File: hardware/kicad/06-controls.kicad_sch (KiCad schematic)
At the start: 38 parts, among them SW1 UP, SW10 SELECT, SW11 L, SW12 R, SW13 MENU, SW2 DOWN, SW3 LEFT, SW4 RIGHT, SW5 A, SW6 B, SW7 X, SW8 Y, SW9 START

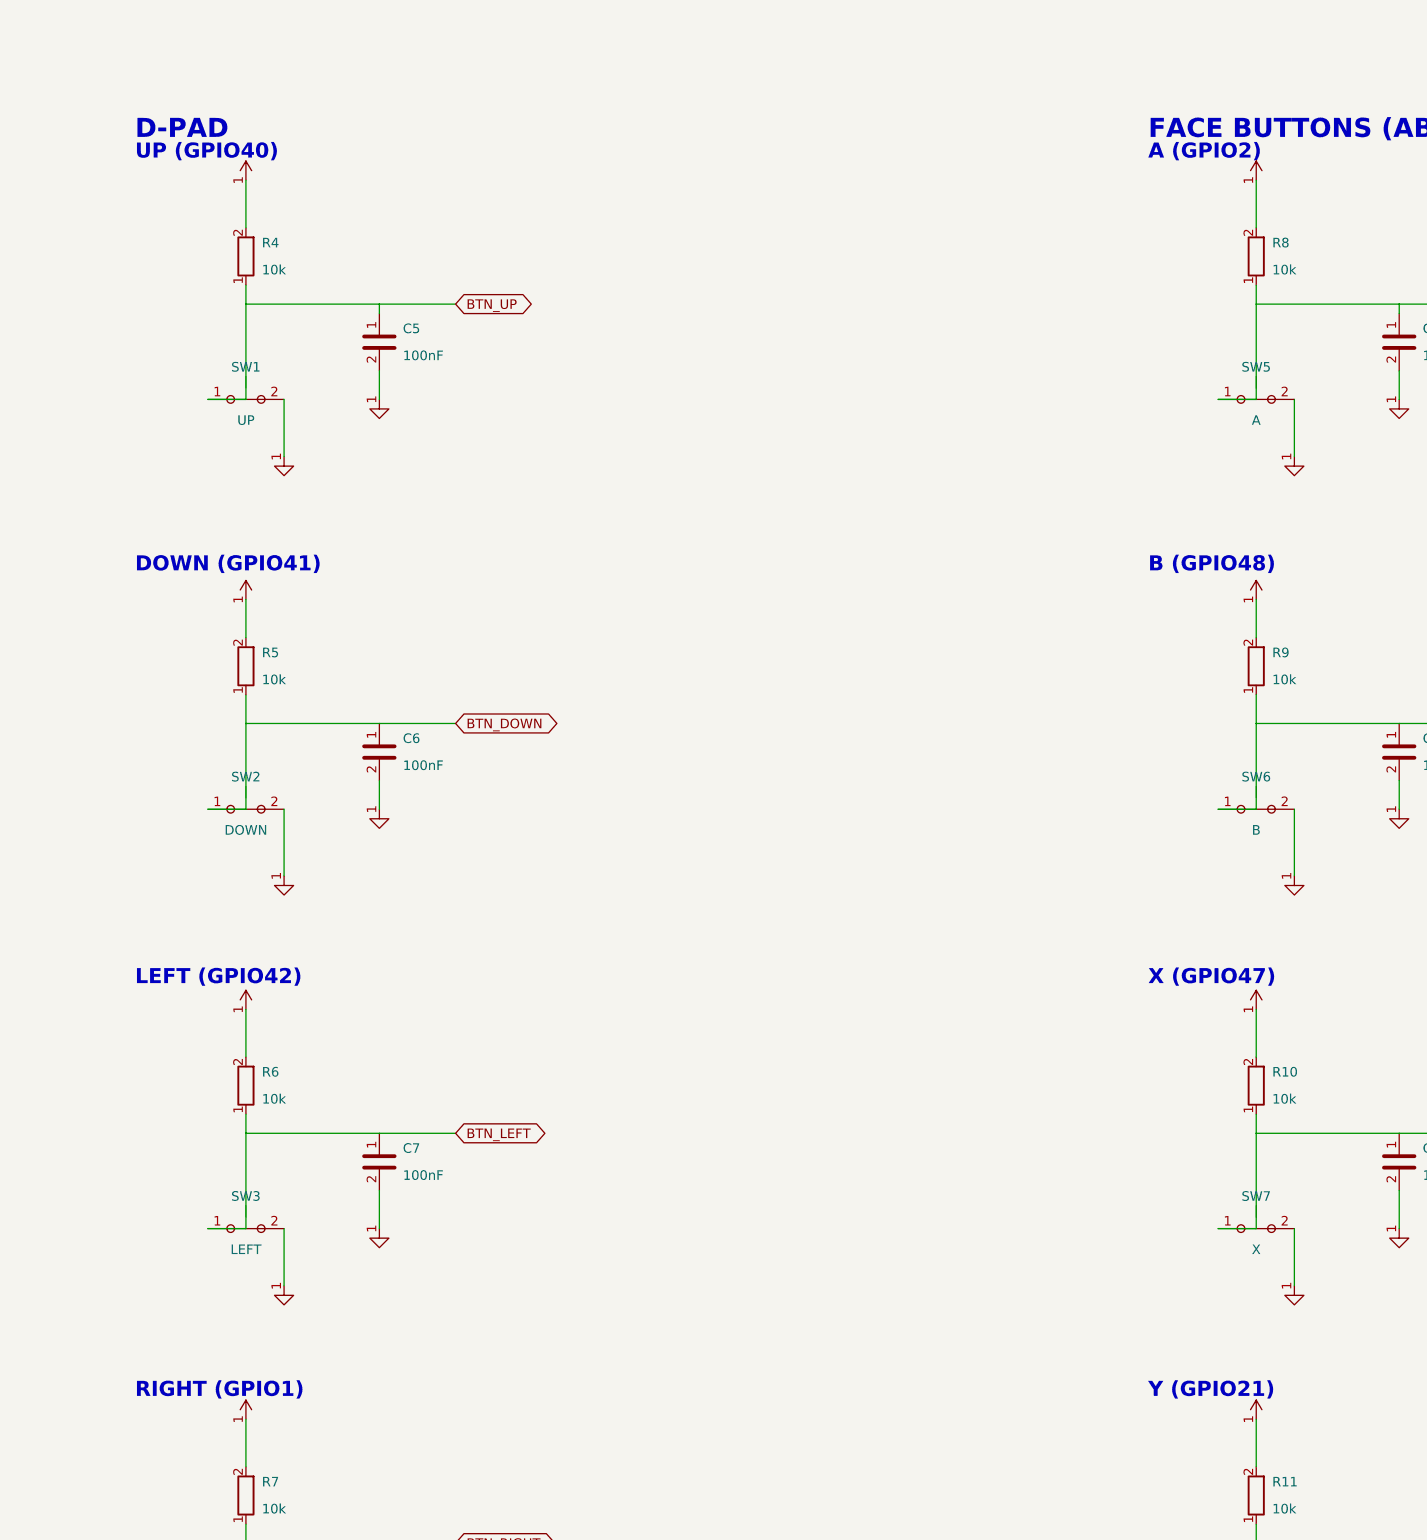
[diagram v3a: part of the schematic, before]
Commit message: Retro-Go first boot on the first article + R39-HIGH-1 (module pins 38/39 swapped)
Phase 2.8 reached: Retro-Go runs on article 0003 — launcher, SD, all 12
buttons, Owlia (NES) and Mario Bros played. Fork fixes are in the
submodule (0e533078, 53878dcb): i80 0x2C/0x3C continuation, landscape
480x320, PDM channel off at volume 0, RIGHT/A swap, L/R in the launcher.

R39-HIGH-1: the WROOM-1 datasheet has pin 38 = IO2 and pin 39 = IO1;
every project table (generator _PIN_TO_GPIO, datasheet_specs, schematic
pin table + symbol, board_config.h, Retro-Go target) had them swapped,
and verify_dfm_v2 asserted the wrong fact. Pins 4-37 re-verified against
the datasheet: only this pair. The copper is right — BTN_RIGHT is on pad
38 = GPIO2, BTN_A on pad 39 = GPIO1 — so the fix is names only:
BTN_RIGHT=GPIO2, BTN_A=GPIO1 everywhere; the regenerated PCB is
byte-identical to the built board; schematics, symbol, bring-up firmware,
net-explorer data and docs regenerated. Gate now asserts 38=GPIO2 and
39=GPIO1. verify-all green, verify_dfa 10/10, retro-go sync 63/63.

Also: prebuilt Retro-Go binaries refreshed, Phase 2 docs switched to
landscape scaling, .gitignore keeps every ROM under test-roms/ out of git
except the committed homebrew set, session log extended.

Co-Authored-By: Claude Opus 5 (1M context) <noreply@anthropic.com>
Claude-Session: https://claude.ai/code/session_01MsWyvkWxko6nCK1kvUkZjV
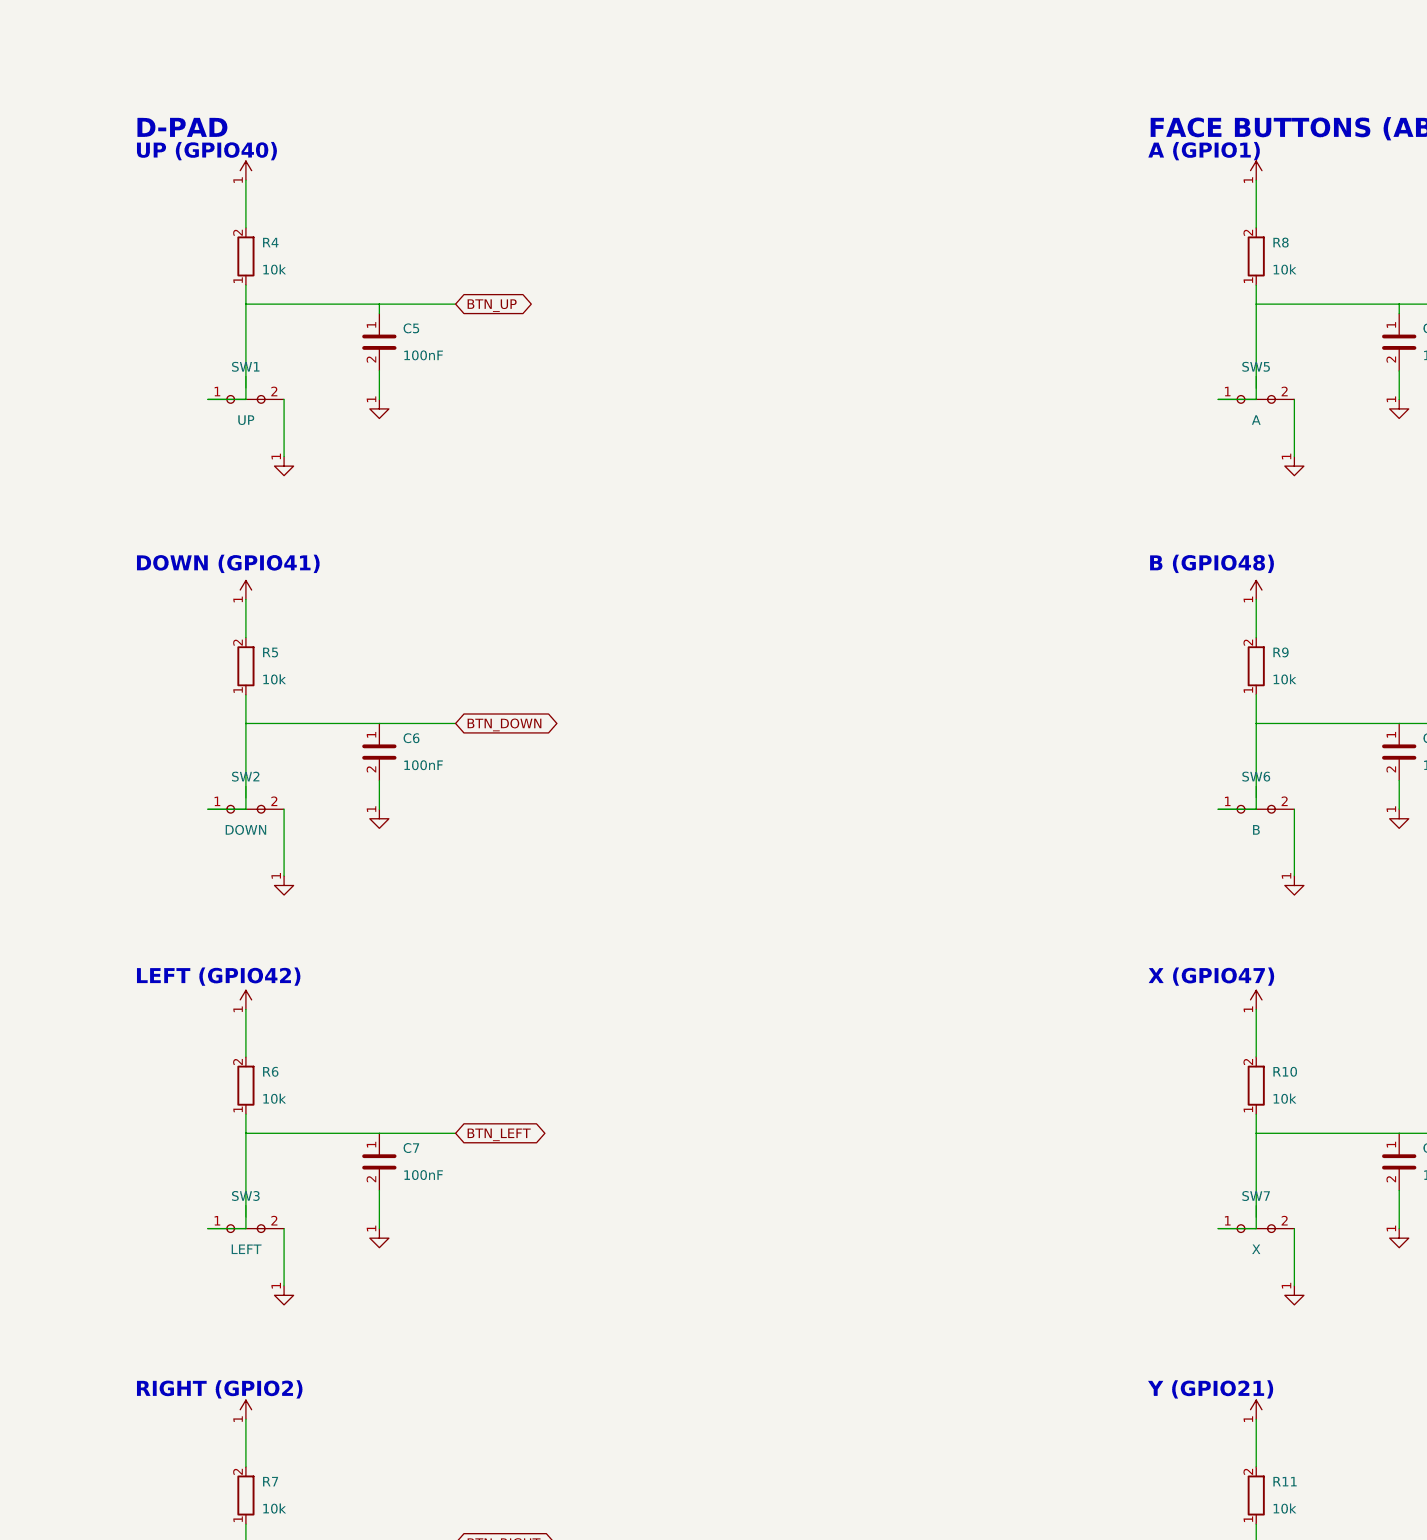
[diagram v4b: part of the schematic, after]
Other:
- note added: "A (GPIO1)"
- note added: "RIGHT (GPIO2)"
- note removed: "A (GPIO2)"
- note removed: "RIGHT (GPIO1)"
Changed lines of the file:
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@@
   (global_label "BTN_LEFT" (shape bidirectional) (at 92.71 186.69 0) (effects (font (size 1.27 1.27))) (property "Intersheetrefs" "" (at 0 0 0) (effects (font (size 1.27 1.27)) hide)))
   (wire (pts (xy 82.55 186.69) (xy 92.71 186.69)) (stroke (width 0) (type default)))
-  (text "RIGHT (GPIO1)" (at 50 221 0) (effects (font (size 2 2) bold) (justify left)))
+  (text "RIGHT (GPIO2)" (at 50 221 0) (effects (font (size 2 2) bold) (justify left)))
   (symbol (lib_id "emu:R") (at 64.77 234.95 180) (unit 1) (exclude_from_sim no) (in_bom yes) (on_board yes) (dnp no) (property "Reference" "R7" (at 66.89 233.15 0) (effects (font (size 1.27 1.27)) (justify right))) (property "Value" "10k" (at 66.89 236.75 0) (effects (font (size 1.27 1.27)) (justify right))) (pin "1") (pin "2") (instances (project "esp32-emu-turbo" (path "/00000007-cafe-4000-8000-000000000007" (reference "R7") (unit 1)) (path "/00000001-cafe-4000-8000-000000000001/00000007-cafe-4000-8000-000000000007" (reference "R7") (unit 1)))))
   (symbol (lib_id "emu:+3V3") (at 64.77 224.79 0) (unit 1) (exclude_from_sim no) (in_bom no) (on_board no) (dnp no) (property "Reference" "#PWR010" (at 64.77 222.79 0) (effects (font (size 1.27 1.27)) hide)) (property "Value" "+3V3" (at 64.77 226.79 0) (effects (font (size 1.27 1.27)) hide)) (pin "1") (instances (project "esp32-emu-turbo" (path "/00000007-cafe-4000-8000-000000000007" (reference "#PWR010") (unit 1)) (path "/00000001-cafe-4000-8000-000000000001/00000007-cafe-4000-8000-000000000007" (reference "#PWR010") (unit 1)))))
@@
   (global_label "BTN_RIGHT" (shape bidirectional) (at 92.71 241.3 0) (effects (font (size 1.27 1.27))) (property "Intersheetrefs" "" (at 0 0 0) (effects (font (size 1.27 1.27)) hide)))
   (wire (pts (xy 82.55 241.3) (xy 92.71 241.3)) (stroke (width 0) (type default)))
-  (text "A (GPIO2)" (at 185 56 0) (effects (font (size 2 2) bold) (justify left)))
+  (text "A (GPIO1)" (at 185 56 0) (effects (font (size 2 2) bold) (justify left)))
   (symbol (lib_id "emu:R") (at 199.39 69.85 180) (unit 1) (exclude_from_sim no) (in_bom yes) (on_board yes) (dnp no) (property "Reference" "R8" (at 201.51 68.05 0) (effects (font (size 1.27 1.27)) (justify right))) (property "Value" "10k" (at 201.51 71.65 0) (effects (font (size 1.27 1.27)) (justify right))) (pin "1") (pin "2") (instances (project "esp32-emu-turbo" (path "/00000007-cafe-4000-8000-000000000007" (reference "R8") (unit 1)) (path "/00000001-cafe-4000-8000-000000000001/00000007-cafe-4000-8000-000000000007" (reference "R8") (unit 1)))))
   (symbol (lib_id "emu:+3V3") (at 199.39 59.69 0) (unit 1) (exclude_from_sim no) (in_bom no) (on_board no) (dnp no) (property "Reference" "#PWR013" (at 199.39 57.69 0) (effects (font (size 1.27 1.27)) hide)) (property "Value" "+3V3" (at 199.39 61.69 0) (effects (font (size 1.27 1.27)) hide)) (pin "1") (instances (project "esp32-emu-turbo" (path "/00000007-cafe-4000-8000-000000000007" (reference "#PWR013") (unit 1)) (path "/00000001-cafe-4000-8000-000000000001/00000007-cafe-4000-8000-000000000007" (reference "#PWR013") (unit 1)))))
